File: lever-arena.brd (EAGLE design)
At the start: 85 x 56 mm, 6 parts, among them Q1 FQP30N06L, Q2 FQP30N06L

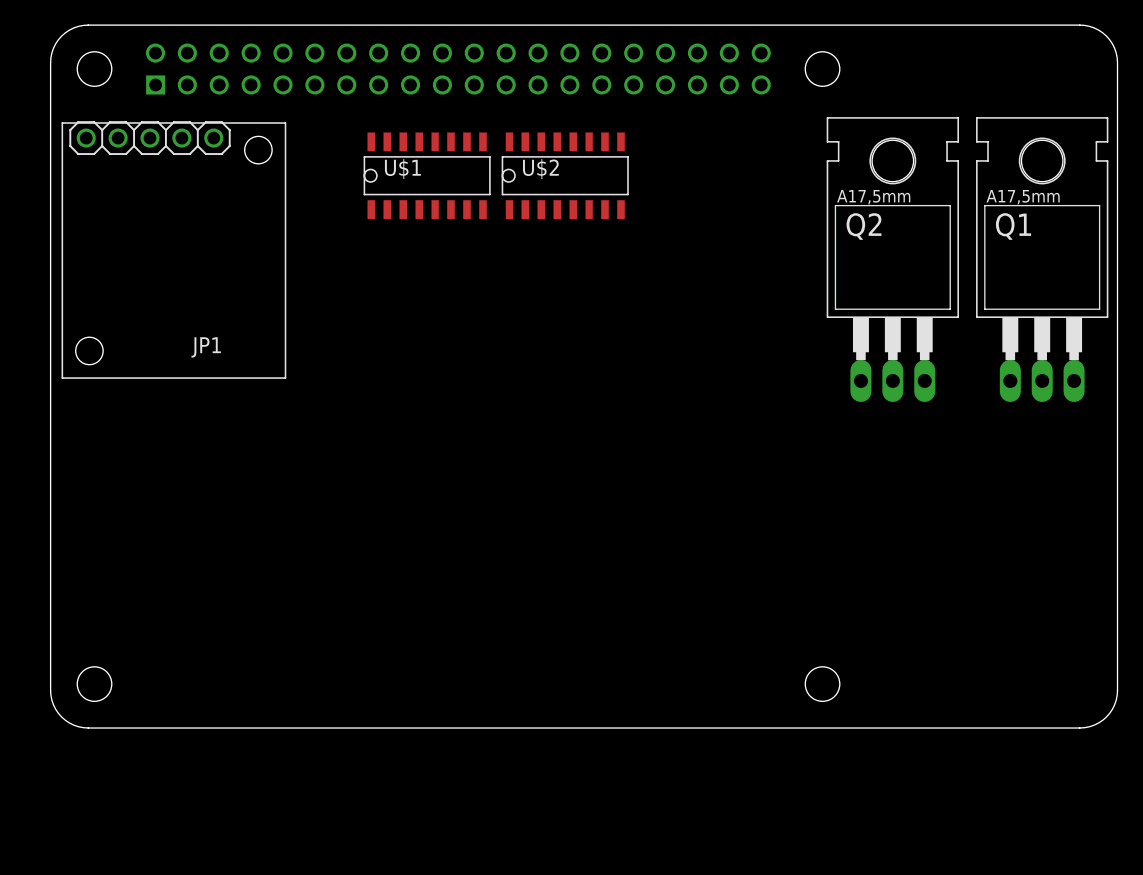
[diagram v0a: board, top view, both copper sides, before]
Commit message: added all components
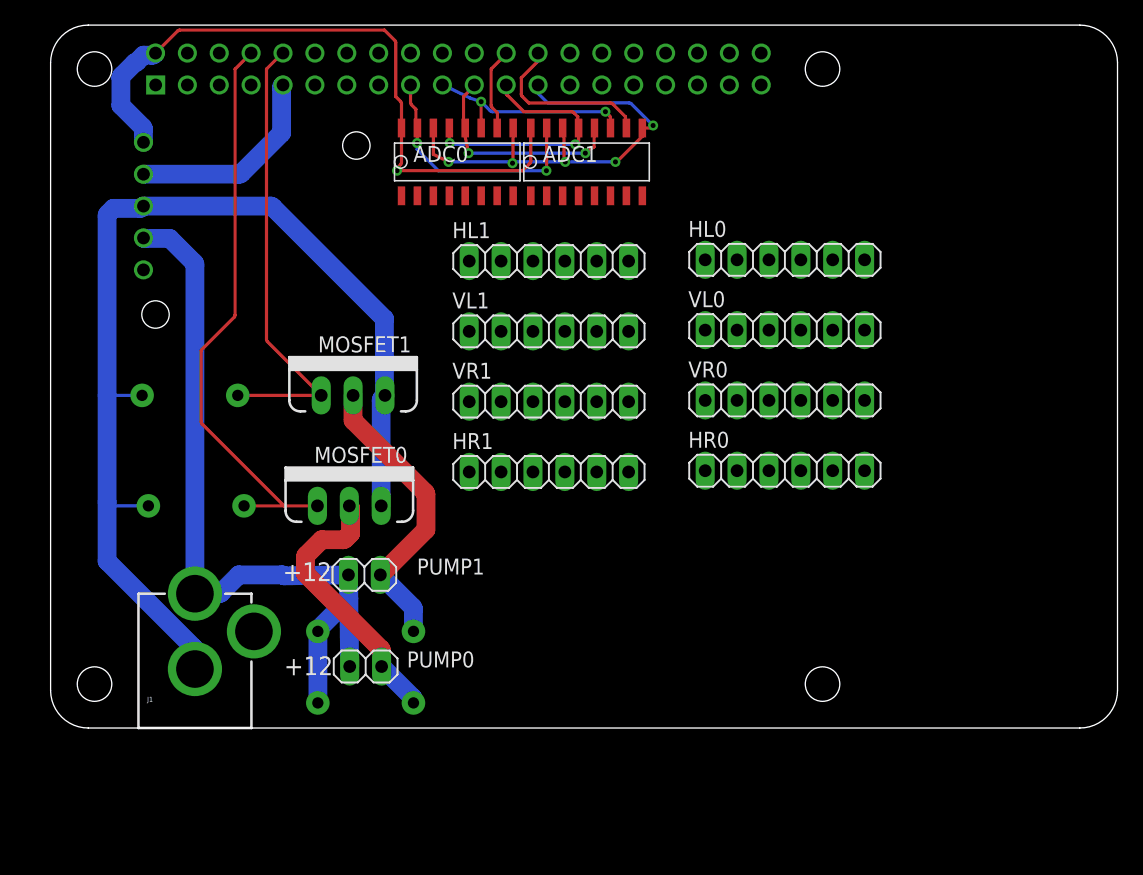
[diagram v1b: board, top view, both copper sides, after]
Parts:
- removed Q1, Q2: FQP30N06L, spencer:TO220
- removed U$1, U$2: MCP3208, spencer:MCP3208-CI/SL
- added ADC0, ADC1: MCP3208, spencer:MCP3208-CI/SL
- added D1, D2: 1N4148, SparkFun-DiscreteSemi:DIODE-1N4148
- added HL0, HL1, HR0, HR1, VL0, VL1, VR0, VR1: (no value), pinhead:1X06
- added J1: POWER_JACKPTH, SparkFun-Connectors:POWER_JACK_PTH
- added MOSFET0, MOSFET1: MOSFET-NCHANNELFQP30N06L, SparkFun-DiscreteSemi:TO220V
- added PUMP0, PUMP1: (no value), pinhead:1X02
- added R1, R2: 10k, SparkFun-Resistors:AXIAL-0.3
- moved JP1 11.9 mm to (7.40, 36.5), flipped to the bottom, turned to 90 degrees
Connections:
- removed net N$2: U$1.AGND
- new net 12V: D1.C, D2.A, D2.C, J1.PWR, JP1.VIN, MOSFET1.2, PUMP0.1, PUMP1.1, PUMP1.2
- new net 3V3: ADC0.VREF, ADC1.VREF, PCB1.P$1, PCB1.P$17
- new net A1: PCB1.P$29
- new net A2: PCB1.P$31
- new net A3: PCB1.P$33
- new net A4: PCB1.P$35
- new net A5: PCB1.P$37
- new net A6: PCB1.P$36
- new net A7: PCB1.P$38
- new net A8: PCB1.P$40
- new net HL0: HL0.3
- new net HL1: HL1.3
- new net HR0: HR0.3
- new net HR1: HR1.3
- new net N$1: ADC1.CH1, VL1.4
- new net N$11: PCB1.P$12
- new net N$12: PCB1.P$14
- new net N$13: PCB1.P$16
- new net N$14: PCB1.P$18
- new net N$15: PCB1.P$20
- new net N$16: PCB1.P$22
- new net N$17: PCB1.P$28
- new net N$18: PCB1.P$30
- new net N$19: PCB1.P$32
- new net N$20: PCB1.P$34
- new net N$21: ADC1.CH3, HR1.4
- new net N$22: ADC1.CH7, HL0.4
- new net N$23: ADC1.CH6, VL0.4
- new net N$24: ADC0.CH5
- new net N$25: ADC0.CH6
- new net N$26: ADC0.CH7
- new net N$27: ADC1.CH5, VR0.4
- new net N$28: ADC1.CH4, HR0.4
- new net N$3: ADC1.CH2, VR1.4
- new net N$30: PCB1.P$27
- new net N$32: PCB1.P$15
- new net N$33: PCB1.P$13
- new net N$34: PCB1.P$11
- new net N$36: PCB1.P$7
- new net N$37: PCB1.P$5
- new net N$38: PCB1.P$3
- new net N$4: D1.A, MOSFET0.2, PUMP0.2
- new net N$48: ADC1.CH0, HL1.4
- new net N$5: ADC0.CH0
- new net N$6: ADC0.CH1
- new net N$7: ADC0.CH2
- new net N$8: JP1.EN
- new net PUMP1: MOSFET0.1, PCB1.P$8, R2.P$1
- new net PUMP2: MOSFET1.1, PCB1.P$10, R1.P$1
- new net VL0: VL0.3
- new net VL1: VL1.3
- new net VR0: VR0.3
- new net VR1: VR1.3
- net 5V: now also ADC0.VDD, ADC1.VDD, HL0.2, HL1.2, HR0.2, HR1.2, VL0.2, VL1.2, VR0.2, VR1.2
- net CE0: now also ADC0.CS; no longer U$1.CS
- net CE1: now also ADC1.CS; no longer U$2.CS
- net GND: now also ADC0.AGND, ADC0.DGND, ADC1.AGND, ADC1.DGND, HL0.1, HL1.1, HR0.1, HR1.1, J1.GND, MOSFET0.3, MOSFET1.3, PCB1.P$25, PCB1.P$39, PCB1.P$9, R1.P$2, R2.P$2, VL0.1, VL1.1, VR0.1, VR1.1
- net MISO: now also ADC0.DOUT, ADC1.DOUT; no longer U$1.DOUT, U$2.DOUT
- net MOSI: now also ADC0.DIN, ADC1.DIN; no longer U$1.DIN, U$2.DIN
- net N$10: now also ADC0.CH4; no longer U$2.DGND
- net N$9: now also ADC0.CH3; no longer U$1.DGND
- net SCLK: now also ADC0.CLK, ADC1.CLK; no longer U$1.CLK, U$2.CLK
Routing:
- net GND: track 0.00 -> 140.5 mm, vias 0 -> 5
- net 12V: track 0.00 -> 84.5 mm
- net 5V: track 0.00 -> 54.2 mm, vias 0 -> 1
- net PUMP1: track 0.00 -> 46.3 mm
- net PUMP2: track 0.00 -> 36.3 mm
- net N$4: track 0.00 -> 21.8 mm
- net SCLK: track 0.00 -> 20.7 mm, vias 0 -> 2
- net 3V3: track 0.00 -> 19.7 mm, vias 0 -> 2
- net MISO: track 0.00 -> 17.5 mm, vias 0 -> 2
- net MOSI: track 0.00 -> 17.1 mm, vias 0 -> 2
- net CE1: track 0.00 -> 13.8 mm
- net CE0: track 0.00 -> 6.65 mm
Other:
- board text added: "+12"

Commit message: Updated
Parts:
- added JP2, JP3, JP4: (no value), pinhead:1X08
- J1: value POWER_JACKPTH -> POWER_JACKPTH_BREAD; device SparkFun-Connectors:POWER_JACK_PTH -> SparkFun-Connectors:POWER_JACK_PTH_BREAD
- moved HL1 25.3 mm to (49.9, 14.1)
- moved VL1 23.7 mm to (50.0, 10.2)
- moved VR1 22.4 mm to (50.0, 6.10)
- moved HR1 21.1 mm to (50.0, 2.00)
- moved HL0 10.8 mm to (49.9, 30.8)
- moved VL0 9.95 mm to (49.9, 26.7)
- moved VR0 9.28 mm to (49.9, 22.6)
- moved HR0 8.83 mm to (49.9, 18.5)
- moved J1 0.60 mm to (11.5, -3.60)
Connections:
- net A8 renamed N$3
- removed net A1: PCB1.P$29
- removed net A2: PCB1.P$31
- removed net A3: PCB1.P$33
- removed net A4: PCB1.P$35
- removed net A5: PCB1.P$37
- removed net A6: PCB1.P$36
- removed net A7: PCB1.P$38
- removed net N$1: ADC1.CH1, VL1.4
- removed net N$11: PCB1.P$12
- removed net N$12: PCB1.P$14
- removed net N$13: PCB1.P$16
- removed net N$14: PCB1.P$18
- removed net N$15: PCB1.P$20
- removed net N$16: PCB1.P$22
- removed net N$17: PCB1.P$28
- removed net N$18: PCB1.P$30
- removed net N$19: PCB1.P$32
- removed net N$20: PCB1.P$34
- removed net N$21: ADC1.CH3, HR1.4
- removed net N$3 (its old number): ADC1.CH2, VR1.4
- removed net N$30: PCB1.P$27
- removed net N$34: PCB1.P$11
- removed net N$36: PCB1.P$7
- removed net N$37: PCB1.P$5
- removed net N$38: PCB1.P$3
- removed net N$48: ADC1.CH0, HL1.4
- new net N$29: ADC1.CH0, HR1.4
- new net N$31: ADC1.CH1, VR1.4
- net 3V3: no longer PCB1.P$1
- net GND: no longer PCB1.P$39, PCB1.P$6
- net HL0: now also PCB1.P$29
- net HL1: now also PCB1.P$36
- net HR0: now also PCB1.P$33
- net HR1: now also PCB1.P$37
- net N$32: now also ADC1.CH2, VL1.4; no longer PCB1.P$15
- net N$33: now also ADC1.CH3, HL1.4; no longer PCB1.P$13
- net PUMP1: now also PCB1.P$11; no longer PCB1.P$8
- net PUMP2: now also PCB1.P$13; no longer PCB1.P$10
- net VL0: now also PCB1.P$31
- net VL1: now also PCB1.P$35
- net VR0: now also PCB1.P$32
- net VR1: now also PCB1.P$38
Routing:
- net 5V: track 54.2 -> 131.4 mm
- net HR1: track 0.00 -> 61.5 mm
- net VR1: track 0.00 -> 60.4 mm
- net N$29: track 0.00 -> 53.6 mm
- net VL1: track 0.00 -> 53.3 mm
- net HL1: track 0.00 -> 52.5 mm
- net GND: track 140.5 -> 192.3 mm
- net N$31: track 0.00 -> 49.6 mm
- net N$32: track 0.00 -> 45.5 mm
- net HR0: track 0.00 -> 44.9 mm
- net VR0: track 0.00 -> 44.0 mm, vias 0 -> 1
- net N$33: track 0.00 -> 41.5 mm
- net N$28: track 0.00 -> 37.7 mm
- net VL0: track 0.00 -> 37.6 mm
- net N$27: track 0.00 -> 33.7 mm
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
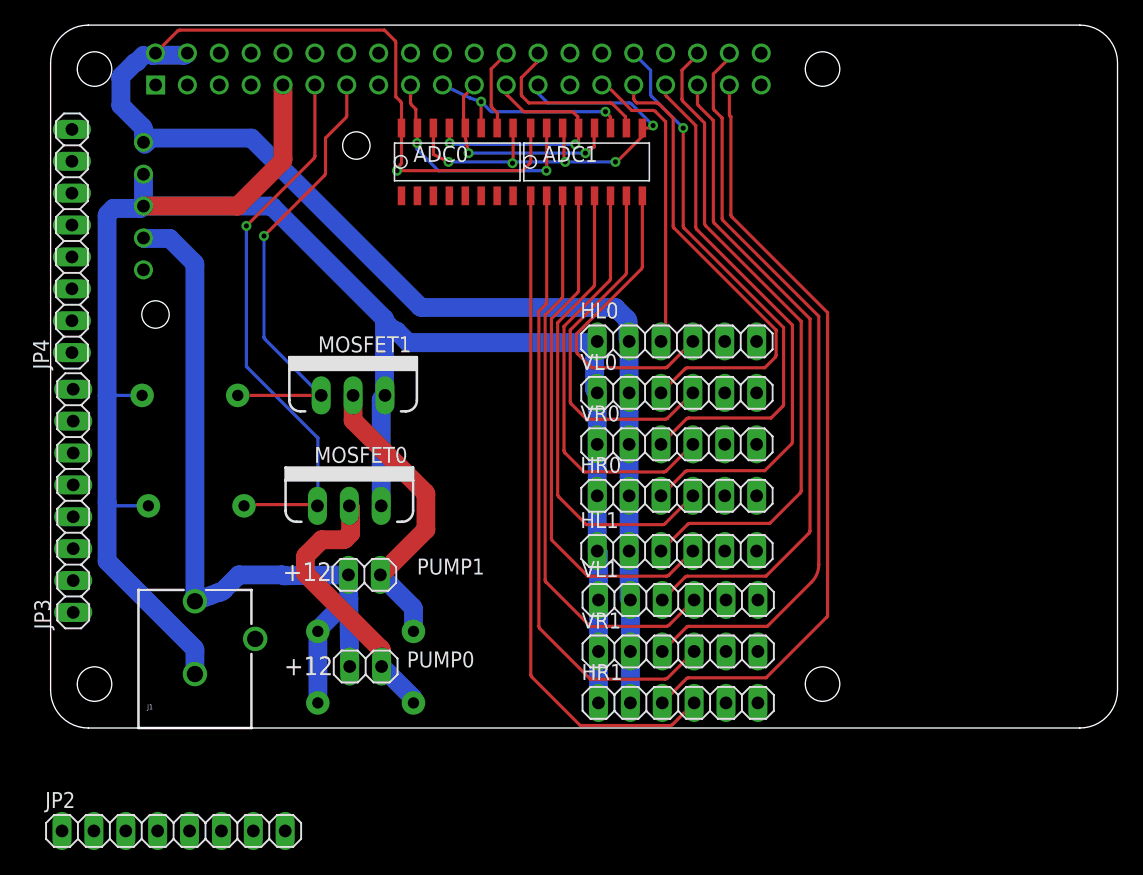
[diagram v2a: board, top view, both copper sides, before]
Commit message: All connectors added
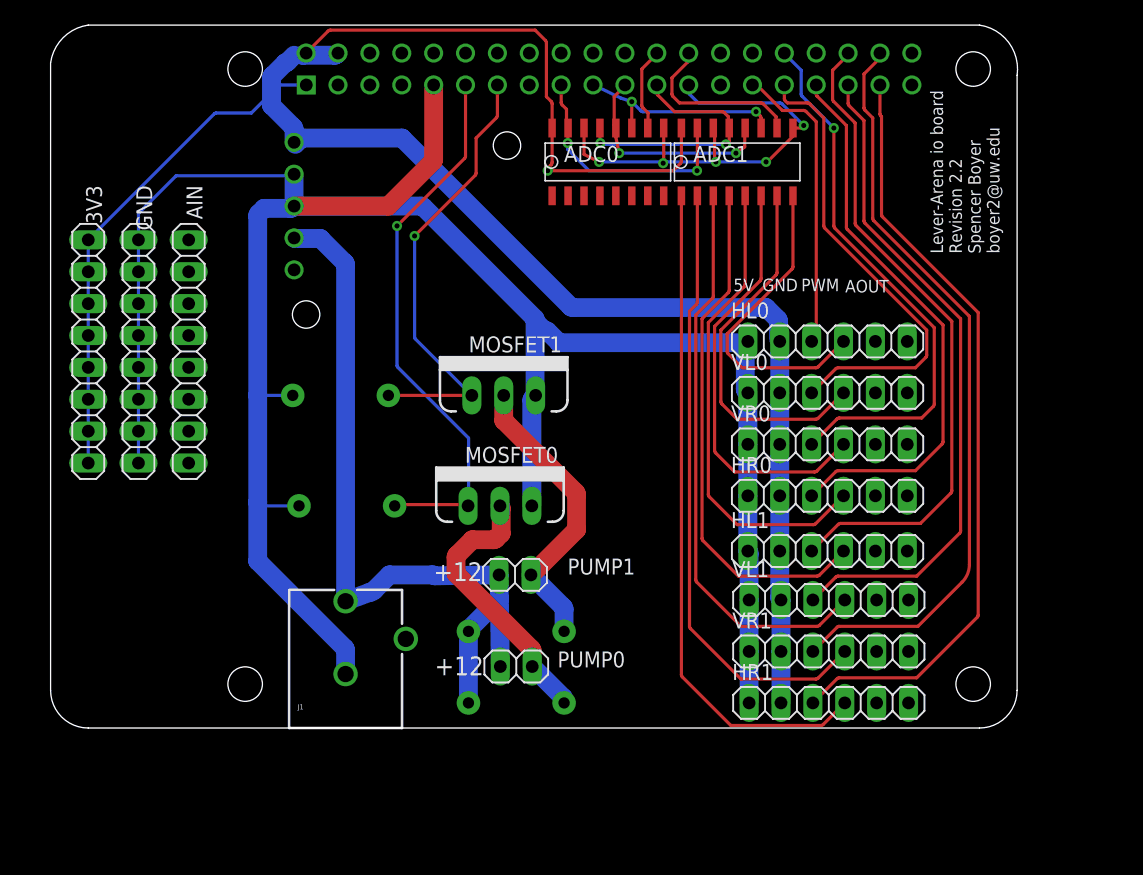
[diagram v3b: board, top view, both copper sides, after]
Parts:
- removed JP2, JP3, JP4: (no value), pinhead:1X08
- added 3V3, AIN, GND: (no value), pinhead:1X08
- moved R1 12.0 mm to (23.1, 26.5)
- moved R2 12.0 mm to (23.6, 17.7)
- moved ADC0 12.0 mm to (44.4, 45.1)
- moved ADC1 12.0 mm to (54.7, 45.1)
- moved D1 12.0 mm to (37.1, 2.00)
- moved D2 12.0 mm to (37.1, 7.70)
- moved HL0 12.0 mm to (61.9, 30.8)
- moved HL1 12.0 mm to (61.9, 14.1)
- moved HR0 12.0 mm to (61.9, 18.5)
- moved HR1 12.0 mm to (62.0, 2.00)
- moved J1 12.0 mm to (23.5, -3.60)
- moved MOSFET1 12.0 mm to (36.1, 26.5)
- moved PCB1 12.0 mm to (12.0, 0.00)
- moved PUMP0 12.0 mm to (37.1, 4.90)
- moved PUMP1 12.0 mm to (37.0, 12.2)
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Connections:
- removed net N$10: ADC0.CH4
- removed net N$24: ADC0.CH5
- removed net N$25: ADC0.CH6
- removed net N$26: ADC0.CH7
- removed net N$5: ADC0.CH0
- removed net N$6: ADC0.CH1
- removed net N$7: ADC0.CH2
- removed net N$9: ADC0.CH3
- new net N$1: ADC0.CH0, AIN.1
- new net N$11: ADC0.CH1, AIN.2
- new net N$12: ADC0.CH2, AIN.3
- new net N$13: ADC0.CH3, AIN.4
- new net N$14: ADC0.CH4, AIN.5
- new net N$15: ADC0.CH5, AIN.6
- new net N$16: ADC0.CH6, AIN.7
- new net N$17: ADC0.CH7, AIN.8
- net 3V3: now also 3V3.1, 3V3.2, 3V3.3, 3V3.4, 3V3.5, 3V3.6, 3V3.7, 3V3.8, PCB1.P$1
- net GND: now also GND.1, GND.2, GND.3, GND.4, GND.5, GND.6, GND.7, GND.8
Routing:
- net 3V3: track 19.7 -> 60.0 mm
- net GND: track 192.3 -> 225.9 mm
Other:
- board size 85 x 56 mm -> 77 x 56 mm
- board text added: "5V"
- board text added: "AOUT"
- board text added: "GND"
- board text added: "Lever-Arena io board Revision 2.2 Spencer Boyer boyer2@uw.edu"
- board text added: "PWM"

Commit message: REVISION 2.2
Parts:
- 3V3: value (none) -> 3v3
- AIN: value (none) -> AIN
- GND: value (none) -> GND
- HL0: value (none) -> HL0
- HL1: value (none) -> HL1
- HR0: value (none) -> HR0
- HR1: value (none) -> HR1
- PUMP0: value (none) -> PUMP0
- PUMP1: value (none) -> PUMP1
- REGULATOR: value (none) -> REGULATOR
- VL0: value (none) -> VL0
- VL1: value (none) -> VL1
- VR0: value (none) -> VR0
- VR1: value (none) -> VR1
- renumbered JP1 to REGULATOR
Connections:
- removed net N$3: PCB1.P$40
- removed net N$8: REGULATOR.EN
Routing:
- net N$16: track 0.00 -> 59.0 mm
- net N$17: track 0.00 -> 48.6 mm
- net N$15: track 0.00 -> 45.1 mm
- net N$14: track 0.00 -> 43.2 mm
- net N$13: track 0.00 -> 43.0 mm
- net N$12: track 0.00 -> 37.9 mm
- net N$11: track 0.00 -> 33.8 mm
- net N$1: track 0.00 -> 31.2 mm
